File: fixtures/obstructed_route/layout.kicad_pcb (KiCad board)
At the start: 2 copper layers, 30 x 12 mm, 3 parts

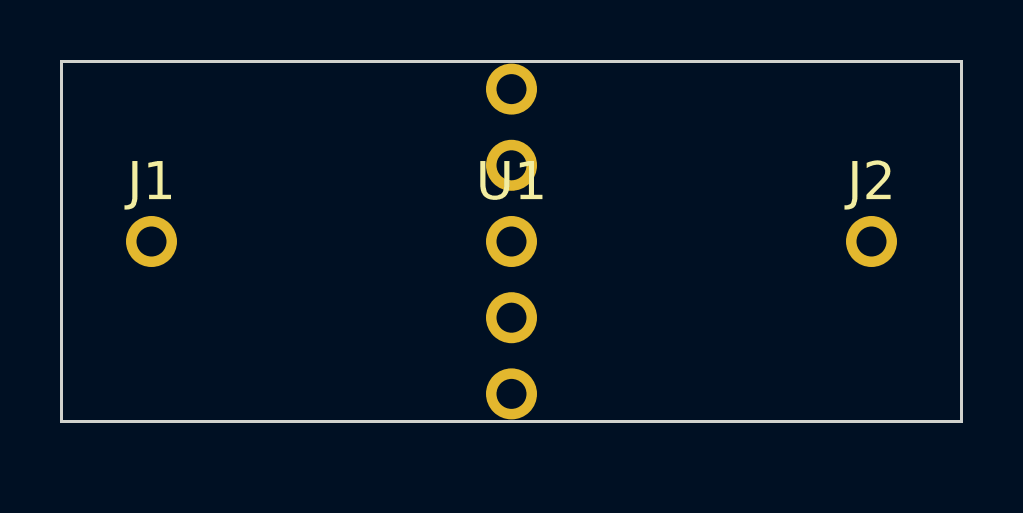
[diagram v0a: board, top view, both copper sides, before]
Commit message: Correct obstruction fixture height without weakening board rules
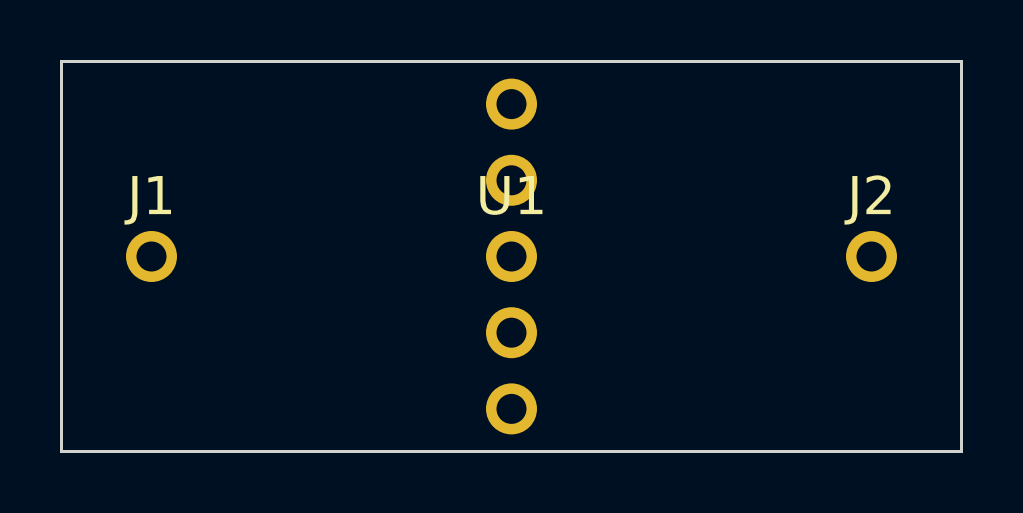
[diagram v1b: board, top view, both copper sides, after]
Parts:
- moved J1 0.50 mm to (3.00, 6.50)
- moved J2 0.50 mm to (27.0, 6.50)
- moved U1 0.50 mm to (15.0, 6.50)
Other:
- board size 30 x 12 mm -> 30 x 13 mm
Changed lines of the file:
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@@
 	(footprint "fixture:THT"
 		(layer "F.Cu")
-		(at 15 6)
+		(at 15 6.5)
 		(property "Reference" "U1"
 			(at 0 -2 0)
@@
 	(footprint "fixture:THT"
 		(layer "F.Cu")
-		(at 3 6)
+		(at 3 6.5)
 		(property "Reference" "J1"
 			(at 0 -2 0)
@@
 	(footprint "fixture:THT"
 		(layer "F.Cu")
-		(at 27 6)
+		(at 27 6.5)
 		(property "Reference" "J2"
 			(at 0 -2 0)
@@
 	(gr_rect
 		(start 0 0)
-		(end 30 12)
+		(end 30 13)
 		(stroke
 			(width 0.1)
